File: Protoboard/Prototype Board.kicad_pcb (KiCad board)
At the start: 2 copper layers, 99.1 x 99.1 mm, 902 parts, among them J1 Conn_01x03_Male, J10 Conn_01x01, J11 Conn_01x01, J12 Conn_01x01, J13 Conn_01x01, J14 Conn_01x01, J15 Conn_01x01, J16 Conn_01x01, J17 Conn_01x01, J18 Conn_01x01, J19 Conn_01x01, J2 Conn_01x03_Male, J20 Conn_01x01, J21 Conn_01x01, J22 Conn_01x01, J23 Conn_01x01, J24 Conn_01x01, J25 Conn_01x01, J26 Conn_01x01, J27 Conn_01x01, J28 Conn_01x01, J29 Conn_01x01, J3 Conn_01x03_Male, J30 Conn_01x01, J31 Conn_01x01, J32 Conn_01x01, J33 Conn_01x01, J34 Conn_01x01, J4 Conn_01x03_Male, J5 Conn_01x01, J6 Conn_01x01, J7 Conn_01x01, J8 Conn_01x01, J9 Conn_01x01, SW1 SW_Push_Dual, SW2 SW_Push_Dual, SW3 SW_Push_Dual, SW4 SW_Push_Dual, SW5 SW_Push_Dual, SW6 SW_Push_Dual

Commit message: Protoboard edits
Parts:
- removed the G*** at (139.7, 35.6)

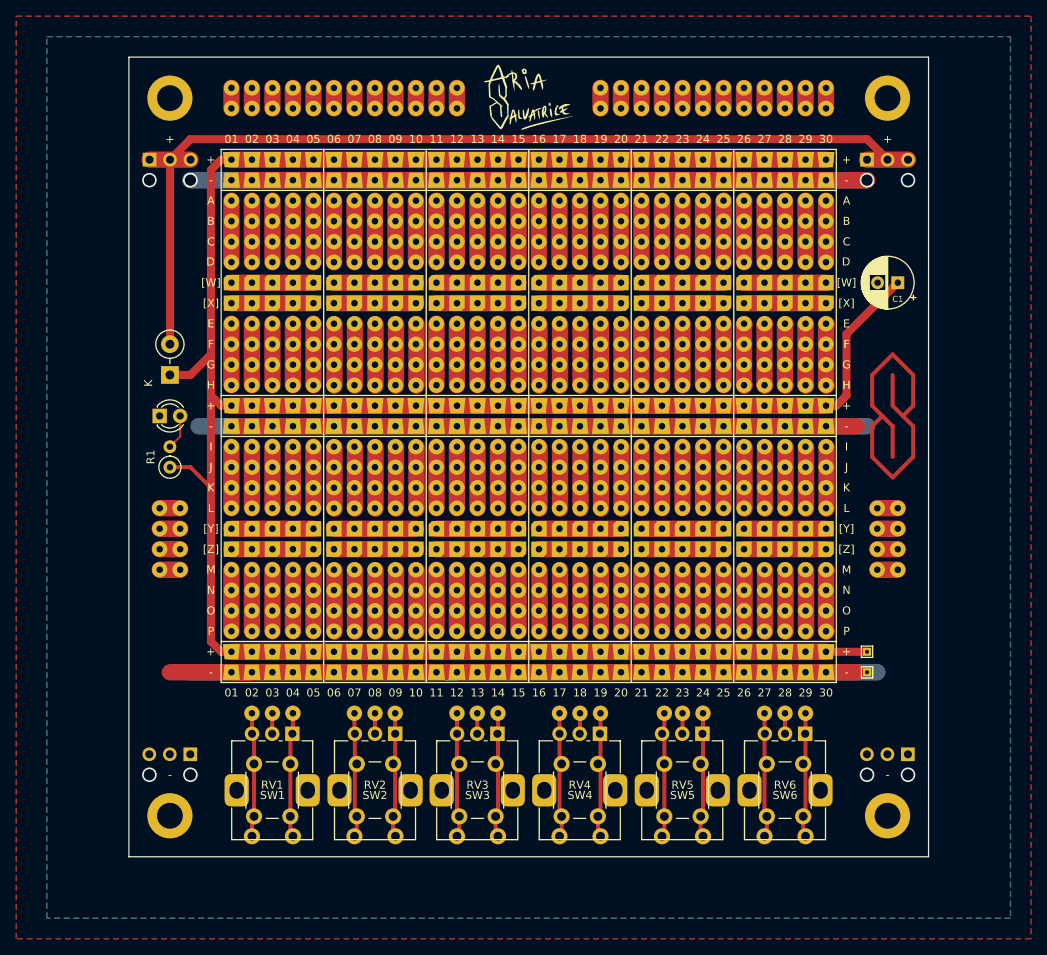
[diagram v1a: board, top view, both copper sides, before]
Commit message: Improve Protoboard Rev2
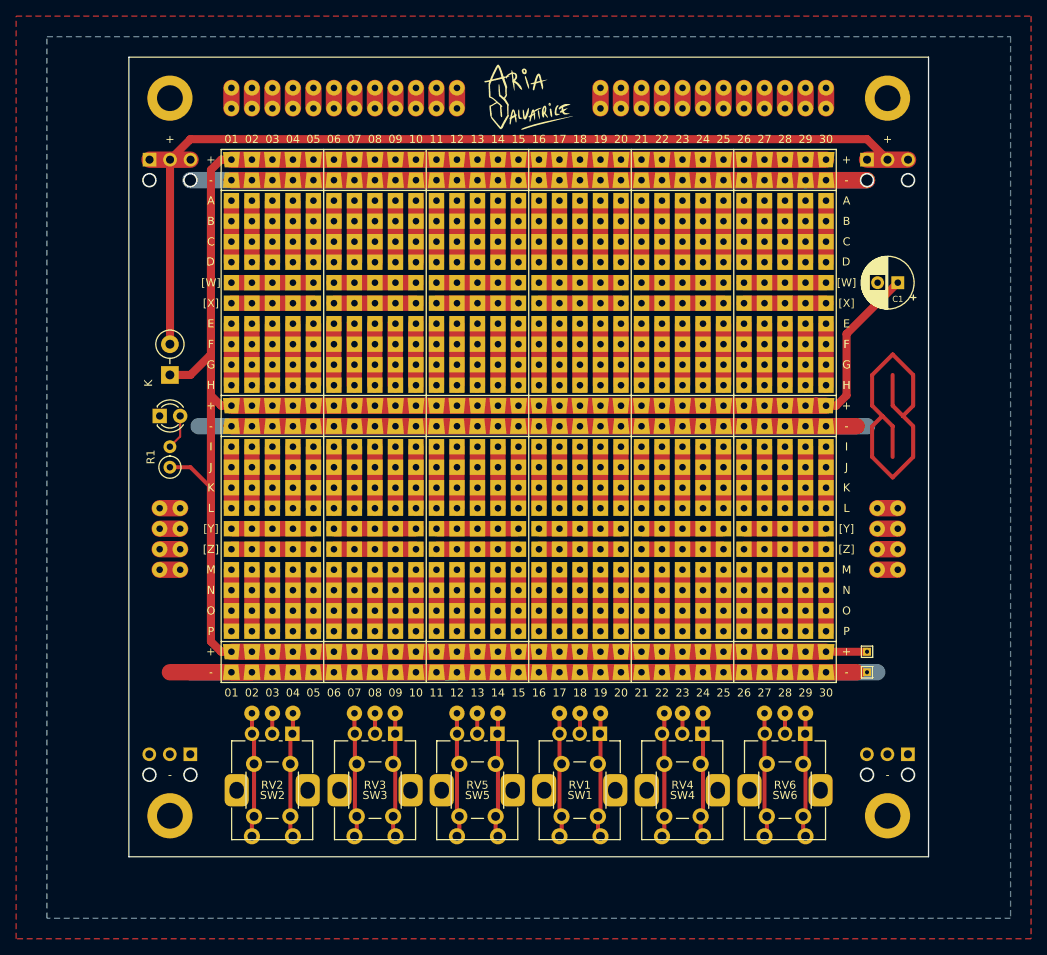
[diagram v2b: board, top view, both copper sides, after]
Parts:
- removed the REF** at (104.1, 78.7)
- removed the REF** at (104.1, 48.3)
- removed REF**1 (x2), REF**10 (x2), REF**100 (x2), REF**101 (x2), REF**102 (x2), REF**103 (x2), REF**104 (x2), REF**105 (x2), REF**106 (x2), REF**107 (x2), REF**108 (x2), REF**109 (x2), REF**11 (x2), REF**110 (x2), REF**111 (x2), REF**112 (x2), REF**113 (x2), REF**114 (x2), REF**115 (x2), REF**116 (x2), REF**117 (x2), REF**118 (x2), REF**119 (x2), REF**12 (x2), REF**120 (x2), REF**121 (x2), REF**122 (x2), REF**123 (x2), REF**124 (x2), REF**125 (x2), REF**126 (x2), REF**127 (x2), REF**128 (x2), REF**129 (x2), REF**13 (x2), REF**130 (x2), REF**131 (x2), REF**132 (x2), REF**133 (x2), REF**134 (x2), REF**135 (x2), REF**136 (x2), REF**137 (x2), REF**138 (x2), REF**139 (x2), REF**14 (x2), REF**140 (x2), REF**141 (x2), REF**142 (x2), REF**143 (x2), REF**144 (x2), REF**145 (x2), REF**146 (x2), REF**147 (x2), REF**148 (x2), REF**149 (x2), REF**15 (x2), REF**150 (x2), REF**151 (x2), REF**152 (x2), REF**153 (x2), REF**154 (x2), REF**155 (x2), REF**156 (x2), REF**157 (x2), REF**158 (x2), REF**159 (x2), REF**16 (x2), REF**160 (x2), REF**161 (x2), REF**162 (x2), REF**163 (x2), REF**164 (x2), REF**165 (x2), REF**166 (x2), REF**167 (x2), REF**168 (x2), REF**169 (x2), REF**17 (x2), REF**170 (x2), REF**171 (x2), REF**172 (x2), REF**173 (x2), REF**174 (x2), REF**175 (x2), REF**176 (x2), REF**177 (x2), REF**178 (x2), REF**179 (x2), REF**18 (x2), REF**180 (x2), REF**181 (x2), REF**182 (x2), REF**183 (x2), REF**184 (x2), REF**185 (x2), REF**186 (x2), REF**187 (x2), REF**188 (x2), REF**189 (x2), REF**19 (x2), REF**190 (x2), REF**191 (x2), REF**192 (x2), REF**193 (x2), REF**194 (x2), REF**195 (x2), REF**196 (x2), REF**197 (x2), REF**198 (x2), REF**199 (x2), REF**2 (x2), REF**20 (x2), REF**200 (x2), REF**201 (x2), REF**202 (x2), REF**203 (x2), REF**204 (x2), REF**205 (x2), REF**206 (x2), REF**207 (x2), REF**208 (x2), REF**209 (x2), REF**21 (x2), REF**210 (x2), REF**211 (x2), REF**212 (x2), REF**213 (x2), REF**214 (x2), REF**215 (x2), REF**216 (x2), REF**217 (x2), REF**218 (x2), REF**219 (x2), REF**22 (x2), REF**220 (x2), REF**221 (x2), REF**222 (x2), REF**223 (x2), REF**224 (x2), REF**225 (x2), REF**226 (x2), REF**227 (x2), REF**228 (x2), REF**229 (x2), REF**23 (x2), REF**230 (x2), REF**231 (x2), REF**232 (x2), REF**233 (x2), REF**234 (x2), REF**235 (x2), REF**236 (x2), REF**237 (x2), REF**238 (x2), REF**239 (x2), REF**24 (x2), REF**240 (x2), REF**241 (x2), REF**242 (x2), REF**243 (x2), REF**244 (x2), REF**245 (x2), REF**246 (x2), REF**247 (x2), REF**248 (x2), REF**249 (x2), REF**25 (x2), REF**250 (x2), REF**251 (x2), REF**252 (x2), REF**253 (x2), REF**254 (x2), REF**255 (x2), REF**256 (x2), REF**257 (x2), REF**258 (x2), REF**259 (x2), REF**26 (x2), REF**260 (x2), REF**261 (x2), REF**262 (x2), REF**263 (x2), REF**264 (x2), REF**265 (x2), REF**266 (x2), REF**267 (x2), REF**268 (x2), REF**269 (x2), REF**27 (x2), REF**270 (x2), REF**271 (x2), REF**272 (x2), REF**273 (x2), REF**274 (x2), REF**275 (x2), REF**276 (x2), REF**277 (x2), REF**278 (x2), REF**279 (x2), REF**28 (x2), REF**280 (x2), REF**281 (x2), REF**282 (x2), REF**283 (x2), REF**284 (x2), REF**285 (x2), REF**286 (x2), REF**287 (x2), REF**288 (x2), REF**289 (x2), REF**29 (x2), REF**290 (x2), REF**291 (x2), REF**292 (x2), REF**293 (x2), REF**294 (x2), REF**295 (x2), REF**296 (x2), REF**297 (x2), REF**298 (x2), REF**299 (x2), REF**3 (x2), REF**30 (x2), REF**31 (x2), REF**32 (x2), REF**33 (x2), REF**34 (x2), REF**35 (x2), REF**36 (x2), REF**37 (x2), REF**38 (x2), REF**39 (x2), REF**4 (x2), REF**40 (x2), REF**41 (x2), REF**42 (x2), REF**43 (x2), REF**44 (x2), REF**45 (x2), REF**46 (x2), REF**47 (x2), REF**48 (x2), REF**49 (x2), REF**5 (x2), REF**50 (x2), REF**51 (x2), REF**52 (x2), REF**53 (x2), REF**54 (x2), REF**55 (x2), REF**56 (x2), REF**57 (x2), REF**58 (x2), REF**59 (x2), REF**6 (x2), REF**60 (x2), REF**61 (x2), REF**62 (x2), REF**63 (x2), REF**64 (x2), REF**65 (x2), REF**66 (x2), REF**67 (x2), REF**68 (x2), REF**69 (x2), REF**7 (x2), REF**70 (x2), REF**71 (x2), REF**72 (x2), REF**73 (x2), REF**74 (x2), REF**75 (x2), REF**76 (x2), REF**77 (x2), REF**78 (x2), REF**79 (x2), REF**8 (x2), REF**80 (x2), REF**81 (x2), REF**82 (x2), REF**83 (x2), REF**84 (x2), REF**85 (x2), REF**86 (x2), REF**87 (x2), REF**88 (x2), REF**89 (x2), REF**9 (x2), REF**90 (x2), REF**91 (x2), REF**92 (x2), REF**93 (x2), REF**94 (x2), REF**95 (x2), REF**96 (x2), REF**97 (x2), REF**98 (x2), REF**99 (x2): PBH, ao_tht:Perf_Board_Hole
- added J100: Connectable_Pad_Group_01x04, Protoboard:Connectable_Pad_Group_01x04, F.Cu at (111.8, 78.7)
- added J101: Connectable_Pad_Group_01x04, Protoboard:Connectable_Pad_Group_01x04, F.Cu at (114.3, 78.7)
- added J102: Connectable_Pad_Group_01x04, Protoboard:Connectable_Pad_Group_01x04, F.Cu at (116.8, 78.7)
- added J103: Connectable_Pad_Group_01x04, Protoboard:Connectable_Pad_Group_01x04, F.Cu at (119.4, 78.7)
- added J104: Connectable_Pad_Group_01x04, Protoboard:Connectable_Pad_Group_01x04, F.Cu at (121.9, 78.7)
- added J105: Connectable_Pad_Group_01x04, Protoboard:Connectable_Pad_Group_01x04, F.Cu at (124.5, 78.7)
- added J106: Connectable_Pad_Group_01x04, Protoboard:Connectable_Pad_Group_01x04, F.Cu at (127.0, 78.7)
- added J107: Connectable_Pad_Group_01x04, Protoboard:Connectable_Pad_Group_01x04, F.Cu at (129.5, 78.7)
- added J108: Connectable_Pad_Group_01x04, Protoboard:Connectable_Pad_Group_01x04, F.Cu at (132.1, 78.7)
- added J109: Connectable_Pad_Group_01x04, Protoboard:Connectable_Pad_Group_01x04, F.Cu at (134.6, 78.7)
- added J110: Connectable_Pad_Group_01x04, Protoboard:Connectable_Pad_Group_01x04, F.Cu at (137.2, 78.7)
- added J111: Connectable_Pad_Group_01x04, Protoboard:Connectable_Pad_Group_01x04, F.Cu at (139.7, 78.7)
- added J112: Connectable_Pad_Group_01x04, Protoboard:Connectable_Pad_Group_01x04, F.Cu at (142.2, 78.7)
- added J113: Connectable_Pad_Group_01x04, Protoboard:Connectable_Pad_Group_01x04, F.Cu at (144.8, 78.7)
- added J114: Connectable_Pad_Group_01x04, Protoboard:Connectable_Pad_Group_01x04, F.Cu at (147.3, 78.7)
- added J115: Connectable_Pad_Group_01x04, Protoboard:Connectable_Pad_Group_01x04, F.Cu at (149.9, 78.7)
- added J116: Connectable_Pad_Group_01x04, Protoboard:Connectable_Pad_Group_01x04, F.Cu at (152.4, 78.7)
- added J117: Connectable_Pad_Group_01x04, Protoboard:Connectable_Pad_Group_01x04, F.Cu at (154.9, 78.7)
- added J118: Connectable_Pad_Group_01x04, Protoboard:Connectable_Pad_Group_01x04, F.Cu at (157.5, 78.7)
- added J119: Connectable_Pad_Group_01x04, Protoboard:Connectable_Pad_Group_01x04, F.Cu at (160.0, 78.7)
- added J120: Connectable_Pad_Group_01x04, Protoboard:Connectable_Pad_Group_01x04, F.Cu at (162.6, 78.7)
- added J121: Connectable_Pad_Group_01x04, Protoboard:Connectable_Pad_Group_01x04, F.Cu at (165.1, 78.7)
- added J122: Connectable_Pad_Group_01x04, Protoboard:Connectable_Pad_Group_01x04, F.Cu at (167.6, 78.7)
- added J123: Connectable_Pad_Group_01x04, Protoboard:Connectable_Pad_Group_01x04, F.Cu at (170.2, 78.7)
- added J124: Connectable_Pad_Group_01x04, Protoboard:Connectable_Pad_Group_01x04, F.Cu at (172.7, 78.7)
- added J125: Connectable_Pad_Group_01x04, Protoboard:Connectable_Pad_Group_01x04, F.Cu at (175.3, 78.7)
- added J126: Connectable_Pad_Group_01x04, Protoboard:Connectable_Pad_Group_01x04, F.Cu at (177.8, 78.7)
- added J127: ~, Protoboard:Connectable_Pad_Group_02x05, F.Cu at (104.1, 88.9)
- added J128: ~, Protoboard:Connectable_Pad_Group_02x05, F.Cu at (116.8, 88.9)
- added J129: ~, Protoboard:Connectable_Pad_Group_02x05, F.Cu at (129.5, 88.9)
- added J130: ~, Protoboard:Connectable_Pad_Group_02x05, F.Cu at (142.2, 88.9)
- added J131: ~, Protoboard:Connectable_Pad_Group_02x05, F.Cu at (154.9, 88.9)
- added J132: ~, Protoboard:Connectable_Pad_Group_02x05, F.Cu at (167.6, 88.9)
- added J135: Connectable_Pad_Group_01x04, Protoboard:Connectable_Pad_Group_01x04, F.Cu at (104.1, 94.0)
- added J136: Connectable_Pad_Group_01x04, Protoboard:Connectable_Pad_Group_01x04, F.Cu at (106.7, 94.0)
- added J137: Connectable_Pad_Group_01x04, Protoboard:Connectable_Pad_Group_01x04, F.Cu at (109.2, 94.0)
- added J138: Connectable_Pad_Group_01x04, Protoboard:Connectable_Pad_Group_01x04, F.Cu at (111.8, 94.0)
- added J139: Connectable_Pad_Group_01x04, Protoboard:Connectable_Pad_Group_01x04, F.Cu at (114.3, 94.0)
- added J140: Connectable_Pad_Group_01x04, Protoboard:Connectable_Pad_Group_01x04, F.Cu at (116.8, 94.0)
- added J141: Connectable_Pad_Group_01x04, Protoboard:Connectable_Pad_Group_01x04, F.Cu at (119.4, 94.0)
- added J142: Connectable_Pad_Group_01x04, Protoboard:Connectable_Pad_Group_01x04, F.Cu at (121.9, 94.0)
- added J143: Connectable_Pad_Group_01x04, Protoboard:Connectable_Pad_Group_01x04, F.Cu at (124.5, 94.0)
- added J144: Connectable_Pad_Group_01x04, Protoboard:Connectable_Pad_Group_01x04, F.Cu at (127.0, 94.0)
- added J145: Connectable_Pad_Group_01x04, Protoboard:Connectable_Pad_Group_01x04, F.Cu at (129.5, 94.0)
- added J146: Connectable_Pad_Group_01x04, Protoboard:Connectable_Pad_Group_01x04, F.Cu at (132.1, 94.0)
- added J147: Connectable_Pad_Group_01x04, Protoboard:Connectable_Pad_Group_01x04, F.Cu at (134.6, 94.0)
- added J148: Connectable_Pad_Group_01x04, Protoboard:Connectable_Pad_Group_01x04, F.Cu at (137.2, 94.0)
- added J149: Connectable_Pad_Group_01x04, Protoboard:Connectable_Pad_Group_01x04, F.Cu at (139.7, 94.0)
- added J150: Connectable_Pad_Group_01x04, Protoboard:Connectable_Pad_Group_01x04, F.Cu at (142.2, 94.0)
- added J151: Connectable_Pad_Group_01x04, Protoboard:Connectable_Pad_Group_01x04, F.Cu at (144.8, 94.0)
- added J152: Connectable_Pad_Group_01x04, Protoboard:Connectable_Pad_Group_01x04, F.Cu at (147.3, 94.0)
- added J153: Connectable_Pad_Group_01x04, Protoboard:Connectable_Pad_Group_01x04, F.Cu at (149.9, 94.0)
- added J154: Connectable_Pad_Group_01x04, Protoboard:Connectable_Pad_Group_01x04, F.Cu at (152.4, 94.0)
- added J155: Connectable_Pad_Group_01x04, Protoboard:Connectable_Pad_Group_01x04, F.Cu at (154.9, 94.0)
- added J156: Connectable_Pad_Group_01x04, Protoboard:Connectable_Pad_Group_01x04, F.Cu at (157.5, 94.0)
- added J157: Connectable_Pad_Group_01x04, Protoboard:Connectable_Pad_Group_01x04, F.Cu at (160.0, 94.0)
- added J158: Connectable_Pad_Group_01x04, Protoboard:Connectable_Pad_Group_01x04, F.Cu at (162.6, 94.0)
- added J159: Connectable_Pad_Group_01x04, Protoboard:Connectable_Pad_Group_01x04, F.Cu at (165.1, 94.0)
- added J160: Connectable_Pad_Group_01x04, Protoboard:Connectable_Pad_Group_01x04, F.Cu at (167.6, 94.0)
- added J161: Connectable_Pad_Group_01x04, Protoboard:Connectable_Pad_Group_01x04, F.Cu at (170.2, 94.0)
- added J162: Connectable_Pad_Group_01x04, Protoboard:Connectable_Pad_Group_01x04, F.Cu at (172.7, 94.0)
- added J163: Connectable_Pad_Group_01x04, Protoboard:Connectable_Pad_Group_01x04, F.Cu at (175.3, 94.0)
- added J164: Connectable_Pad_Group_01x04, Protoboard:Connectable_Pad_Group_01x04, F.Cu at (177.8, 94.0)
- added J17: Connectable_Pad_Group_01x04, Protoboard:Connectable_Pad_Group_01x04, F.Cu at (104.1, 48.3)
- added J18: Connectable_Pad_Group_01x04, Protoboard:Connectable_Pad_Group_01x04, F.Cu at (106.7, 48.3)
- added J19: Connectable_Pad_Group_01x04, Protoboard:Connectable_Pad_Group_01x04, F.Cu at (109.2, 48.3)
- added J20: Connectable_Pad_Group_01x04, Protoboard:Connectable_Pad_Group_01x04, F.Cu at (111.8, 48.3)
- added J21: Connectable_Pad_Group_01x04, Protoboard:Connectable_Pad_Group_01x04, F.Cu at (114.3, 48.3)
- added J22: Connectable_Pad_Group_01x04, Protoboard:Connectable_Pad_Group_01x04, F.Cu at (116.8, 48.3)
- added J23: Connectable_Pad_Group_01x04, Protoboard:Connectable_Pad_Group_01x04, F.Cu at (119.4, 48.3)
- added J24: Connectable_Pad_Group_01x04, Protoboard:Connectable_Pad_Group_01x04, F.Cu at (121.9, 48.3)
- added J25: Connectable_Pad_Group_01x04, Protoboard:Connectable_Pad_Group_01x04, F.Cu at (124.5, 48.3)
- added J26: Connectable_Pad_Group_01x04, Protoboard:Connectable_Pad_Group_01x04, F.Cu at (127.0, 48.3)
- added J27: Connectable_Pad_Group_01x04, Protoboard:Connectable_Pad_Group_01x04, F.Cu at (129.5, 48.3)
- added J28: Connectable_Pad_Group_01x04, Protoboard:Connectable_Pad_Group_01x04, F.Cu at (132.1, 48.3)
- added J29: Connectable_Pad_Group_01x04, Protoboard:Connectable_Pad_Group_01x04, F.Cu at (134.6, 48.3)
- added J30: Connectable_Pad_Group_01x04, Protoboard:Connectable_Pad_Group_01x04, F.Cu at (137.2, 48.3)
- added J31: Connectable_Pad_Group_01x04, Protoboard:Connectable_Pad_Group_01x04, F.Cu at (139.7, 48.3)
- added J32: Connectable_Pad_Group_01x04, Protoboard:Connectable_Pad_Group_01x04, F.Cu at (142.2, 48.3)
- added J33: Connectable_Pad_Group_01x04, Protoboard:Connectable_Pad_Group_01x04, F.Cu at (144.8, 48.3)
- added J34: Connectable_Pad_Group_01x04, Protoboard:Connectable_Pad_Group_01x04, F.Cu at (147.3, 48.3)
- added J35: Connectable_Pad_Group_01x04, Protoboard:Connectable_Pad_Group_01x04, F.Cu at (149.9, 48.3)
- added J36: Connectable_Pad_Group_01x04, Protoboard:Connectable_Pad_Group_01x04, F.Cu at (152.4, 48.3)
- added J37: Connectable_Pad_Group_01x04, Protoboard:Connectable_Pad_Group_01x04, F.Cu at (154.9, 48.3)
- added J38: Connectable_Pad_Group_01x04, Protoboard:Connectable_Pad_Group_01x04, F.Cu at (157.5, 48.3)
- added J39: Connectable_Pad_Group_01x04, Protoboard:Connectable_Pad_Group_01x04, F.Cu at (160.0, 48.3)
- added J40: Connectable_Pad_Group_01x04, Protoboard:Connectable_Pad_Group_01x04, F.Cu at (162.6, 48.3)
- added J41: Connectable_Pad_Group_01x04, Protoboard:Connectable_Pad_Group_01x04, F.Cu at (165.1, 48.3)
- added J42: Connectable_Pad_Group_01x04, Protoboard:Connectable_Pad_Group_01x04, F.Cu at (167.6, 48.3)
- added J43: Connectable_Pad_Group_01x04, Protoboard:Connectable_Pad_Group_01x04, F.Cu at (170.2, 48.3)
- added J44: Connectable_Pad_Group_01x04, Protoboard:Connectable_Pad_Group_01x04, F.Cu at (172.7, 48.3)
- added J45: Connectable_Pad_Group_01x04, Protoboard:Connectable_Pad_Group_01x04, F.Cu at (175.3, 48.3)
- added J46: Connectable_Pad_Group_01x04, Protoboard:Connectable_Pad_Group_01x04, F.Cu at (177.8, 48.3)
- added J55: ~, Protoboard:Connectable_Pad_Group_02x05, F.Cu at (104.1, 58.4)
- added J56: ~, Protoboard:Connectable_Pad_Group_02x05, F.Cu at (116.8, 58.4)
- added J57: ~, Protoboard:Connectable_Pad_Group_02x05, F.Cu at (129.5, 58.4)
- added J58: ~, Protoboard:Connectable_Pad_Group_02x05, F.Cu at (142.2, 58.4)
- added J59: ~, Protoboard:Connectable_Pad_Group_02x05, F.Cu at (154.9, 58.4)
- added J60: ~, Protoboard:Connectable_Pad_Group_02x05, F.Cu at (167.6, 58.4)
- added J63: Connectable_Pad_Group_01x04, Protoboard:Connectable_Pad_Group_01x04, F.Cu at (104.1, 63.5)
- added J64: Connectable_Pad_Group_01x04, Protoboard:Connectable_Pad_Group_01x04, F.Cu at (106.7, 63.5)
- added J65: Connectable_Pad_Group_01x04, Protoboard:Connectable_Pad_Group_01x04, F.Cu at (109.2, 63.5)
- added J66: Connectable_Pad_Group_01x04, Protoboard:Connectable_Pad_Group_01x04, F.Cu at (111.8, 63.5)
- added J67: Connectable_Pad_Group_01x04, Protoboard:Connectable_Pad_Group_01x04, F.Cu at (114.3, 63.5)
- added J68: Connectable_Pad_Group_01x04, Protoboard:Connectable_Pad_Group_01x04, F.Cu at (116.8, 63.5)
- added J69: Connectable_Pad_Group_01x04, Protoboard:Connectable_Pad_Group_01x04, F.Cu at (119.4, 63.5)
- added J70: Connectable_Pad_Group_01x04, Protoboard:Connectable_Pad_Group_01x04, F.Cu at (121.9, 63.5)
- added J71: Connectable_Pad_Group_01x04, Protoboard:Connectable_Pad_Group_01x04, F.Cu at (124.5, 63.5)
- added J72: Connectable_Pad_Group_01x04, Protoboard:Connectable_Pad_Group_01x04, F.Cu at (127.0, 63.5)
- added J73: Connectable_Pad_Group_01x04, Protoboard:Connectable_Pad_Group_01x04, F.Cu at (129.5, 63.5)
- added J74: Connectable_Pad_Group_01x04, Protoboard:Connectable_Pad_Group_01x04, F.Cu at (132.1, 63.5)
- added J75: Connectable_Pad_Group_01x04, Protoboard:Connectable_Pad_Group_01x04, F.Cu at (134.6, 63.5)
- added J76: Connectable_Pad_Group_01x04, Protoboard:Connectable_Pad_Group_01x04, F.Cu at (137.2, 63.5)
- added J77: Connectable_Pad_Group_01x04, Protoboard:Connectable_Pad_Group_01x04, F.Cu at (139.7, 63.5)
- added J78: Connectable_Pad_Group_01x04, Protoboard:Connectable_Pad_Group_01x04, F.Cu at (142.2, 63.5)
- added J79: Connectable_Pad_Group_01x04, Protoboard:Connectable_Pad_Group_01x04, F.Cu at (144.8, 63.5)
- added J80: Connectable_Pad_Group_01x04, Protoboard:Connectable_Pad_Group_01x04, F.Cu at (147.3, 63.5)
- added J81: Connectable_Pad_Group_01x04, Protoboard:Connectable_Pad_Group_01x04, F.Cu at (149.9, 63.5)
- added J82: Connectable_Pad_Group_01x04, Protoboard:Connectable_Pad_Group_01x04, F.Cu at (152.4, 63.5)
- renumbered D2 to D1, D1 to D2, J20 to J1, J12 to J10, J7 to J11, J13 to J12, J22 to J13, J1 to J133, J3 to J134, J28 to J14, J18 to J15, J33 to J16, J2 to J165, J4 to J166, J35 to J167, J41 to J168, J47 to J169, J53 to J170, J59 to J171, J65 to J172, J71 to J173, J77 to J174, J83 to J175, J89 to J176, J95 to J177, J101 to J178, J107 to J179, J113 to J180, J119 to J181, J125 to J182, J131 to J183, J137 to J184, J143 to J185, J149 to J186, J155 to J187, J161 to J188, J167 to J189, J173 to J190, J179 to J191, J185 to J192, J191 to J193, J197 to J194, J203 to J195, J209 to J196, J36 to J197, J42 to J198, J48 to J199, J26 to J2, J54 to J200, J60 to J201, J66 to J202, J72 to J203, J78 to J204, J84 to J205, J90 to J206, J96 to J207, J102 to J208, J108 to J209, J114 to J210, J120 to J211, J126 to J212, J132 to J213, J138 to J214, J144 to J215, J150 to J216, J156 to J217, J162 to J218, J168 to J219, J174 to J220, J180 to J221, J186 to J222, J192 to J223, J198 to J224, J204 to J225, J210 to J226, J37 to J227, J43 to J228, J49 to J229, J55 to J230, J61 to J231, J67 to J232, J73 to J233, J79 to J234, J85 to J235, J91 to J236, J97 to J237, J103 to J238, J109 to J239, J115 to J240, J121 to J241, J127 to J242, J133 to J243, J139 to J244, J145 to J245, J151 to J246, J157 to J247, J163 to J248, J169 to J249, J175 to J250, J181 to J251, J187 to J252, J193 to J253, J199 to J254, J205 to J255, J211 to J256, J38 to J257, J44 to J258, J50 to J259, J56 to J260, J62 to J261, J68 to J262, J74 to J263, J80 to J264, J86 to J265, J92 to J266, J98 to J267, J104 to J268, J110 to J269, J116 to J270, J122 to J271, J128 to J272, J134 to J273, J140 to J274, J146 to J275, J152 to J276, J158 to J277, J164 to J278, J170 to J279, J176 to J280, J182 to J281, J188 to J282, J194 to J283, J200 to J284, J206 to J285, J212 to J286, J39 to J287, J45 to J288, J51 to J289, J57 to J290, J63 to J291, J69 to J292, J75 to J293, J81 to J294, J87 to J295, J93 to J296, J99 to J297, J105 to J298, J111 to J299, J5 to J3, J117 to J300, J123 to J301, J129 to J302, J135 to J303, J141 to J304, J147 to J305, J153 to J306, J159 to J307, J165 to J308, J171 to J309, J177 to J310, J183 to J311, J189 to J312, J195 to J313, J201 to J314, J207 to J315, J213 to J316, J40 to J317, J46 to J318, J52 to J319, J58 to J320, J64 to J321, J70 to J322, J76 to J323, J82 to J324, J88 to J325, J94 to J326, J100 to J327, J106 to J328, J112 to J329, J118 to J330, J124 to J331, J130 to J332, J136 to J333, J142 to J334, J148 to J335, J154 to J336, J160 to J337, J166 to J338, J172 to J339, J178 to J340, J184 to J341, J190 to J342, J196 to J343, J202 to J344, J208 to J345, J214 to J346, J11 to J4, J8 to J47, J14 to J48, J23 to J49, J32 to J5, J29 to J50, J9 to J51, J15 to J52, J24 to J53, J30 to J54, J17 to J6, J19 to J61, J34 to J62, J21 to J7, J27 to J8, J6 to J9, J10 to J93, J16 to J94, J25 to J95, J31 to J96, RV4 to RV1, RV1 to RV2, RV2 to RV3, RV5 to RV4, RV3 to RV5, SW4 to SW1, SW1 to SW2, SW2 to SW3, SW5 to SW4, SW3 to SW5
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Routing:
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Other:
- board text added: "TODO LIST - Bonus pads not on the schematic - Imported symbol to replace - Rotary encoder?? - Remake the cursed footprints - Redo schematic - Have 3D models - Can I fit in MORE knobs? - Use proper net width (sounds complicated) - Pass DRC lol"
- board text removed: "TODO LIST - Vertical tracks are poorly aligned - Vertical tracks are not on the schematic - Horizontal groups poorly separated visually - Horizontal groups are not on the schematic - Bonus pads not on the schematic - Imported symbol to replace - Move capacitor up? - Rotary encoder?? - Remake the cursed footprints - Redo schematic - Have 3D models - Can I fit in MORE knobs? - Use proper net width 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"

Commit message: Protoboard Rev2 ready soon, needs checking
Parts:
- removed the J167 at (170.2, 43.2)
- removed J168, J169, J170, J171, J172, J173, J193, J194, J195, J196, J197, J198, J214, J215, J216, J217, J218, J219, J220, J221, J222, J223, J224, J225, J226, J227, J228, J229, J230, J231, J232, J233, J234, J235, J236, J237, J238, J239, J240, J241, J242, J243, J244, J245, J246, J247, J248, J249, J250, J251, J252, J253, J254, J255, J256, J257, J258, J259, J260, J261, J262, J263, J264, J265, J266, J267, J268, J269, J270, J271, J272, J273, J274, J275, J276, J277, J278, J279, J280, J281, J282, J283, J284, J285, J286, J287, J288, J289, J290, J291, J292, J293, J294, J295, J296, J297, J298, J299, J300, J301, J302, J303, J304, J305, J306, J307, J308, J309, J310, J311, J312, J313, J314, J315, J316, J317, J318, J319, J320, J321, J322, J323, J324, J325, J326, J327, J328, J329, J330, J331, J332, J333, J334, J335, J336, J337, J338, J339, J340, J341, J342, J343, J344, J345, J346: ~, ao_tht:Perf_Board_Hole
- removed the J174 at (167.6, 43.2)
- removed the J175 at (127.0, 43.2)
- removed the J176 at (142.2, 43.2)
- removed the J177 at (114.3, 43.2)
- removed the J178 at (116.8, 43.2)
- removed the J179 at (149.9, 43.2)
- removed the J180 at (106.7, 43.2)
- removed the J181 at (147.3, 43.2)
- removed the J182 at (172.7, 43.2)
- removed the J183 at (154.9, 43.2)
- removed the J184 at (124.5, 43.2)
- removed the J185 at (119.4, 43.2)
- removed the J186 at (144.8, 43.2)
- removed the J187 at (109.2, 43.2)
- removed the J188 at (152.4, 43.2)
- removed the J189 at (139.7, 43.2)
- removed the J190 at (162.6, 43.2)
- removed the J191 at (132.1, 43.2)
- removed the J192 at (160.0, 43.2)
- removed the J199 at (165.1, 45.7)
- removed the J200 at (137.2, 45.7)
- removed the J201 at (116.8, 45.7)
- removed the J202 at (144.8, 45.7)
- removed the J203 at (127.0, 45.7)
- removed the J204 at (157.5, 45.7)
- removed the J205 at (149.9, 45.7)
- removed the J206 at (124.5, 45.7)
- removed the J207 at (114.3, 45.7)
- removed the J208 at (175.3, 45.7)
- removed the J209 at (104.1, 45.7)
- removed the J210 at (139.7, 45.7)
- removed the J211 at (106.7, 45.7)
- removed the J212 at (160.0, 45.7)
- removed the J213 at (109.2, 45.7)
- removed the REF** at (177.8, 34.3)
- removed the REF** at (132.1, 34.3)
- removed the REF** at (95.2, 91.4)
- removed the REF** at (121.9, 36.8)
- removed the REF** at (152.4, 34.3)
- removed the REF** at (184.2, 94.0)
- removed the REF** at (97.8, 91.4)
- removed the REF** at (167.6, 36.8)
- removed the REF** at (97.8, 94.0)
- removed the REF** at (152.4, 36.8)
- removed the REF** at (114.3, 34.3)
- removed the REF** at (160.0, 34.3)
- removed the REF** at (184.2, 88.9)
- removed the REF** at (175.3, 36.8)
- removed the REF** at (172.7, 34.3)
- removed the REF** at (95.2, 86.4)
- removed the REF** at (170.2, 34.3)
- removed the REF** at (129.5, 34.3)
- removed the REF** at (175.3, 34.3)
- removed the REF** at (154.9, 34.3)
- removed the REF** at (109.2, 34.3)
- removed the REF** at (111.8, 34.3)
- removed the REF** at (119.4, 34.3)
- removed the REF** at (116.8, 34.3)
- removed the REF** at (165.1, 36.8)
- removed the REF** at (184.2, 91.4)
- removed the REF** at (119.4, 36.8)
- removed the REF** at (157.5, 36.8)
- removed the REF** at (160.0, 36.8)
- removed the REF** at (186.7, 94.0)
- removed the REF** at (170.2, 36.8)
- removed the REF** at (154.9, 36.8)
- removed the REF** at (132.1, 36.8)
- removed the REF** at (124.5, 36.8)
- removed the REF** at (95.2, 88.9)
- removed the REF** at (127.0, 36.8)
- removed the REF** at (172.7, 36.8)
- removed the REF** at (149.9, 34.3)
- removed the REF** at (111.8, 36.8)
- removed the REF** at (186.7, 91.4)
- removed the REF** at (97.8, 86.4)
- removed the REF** at (106.7, 34.3)
- removed the REF** at (129.5, 36.8)
- removed the REF** at (177.8, 36.8)
- removed the REF** at (186.7, 86.4)
- removed the REF** at (116.8, 36.8)
- removed the REF** at (97.8, 88.9)
- removed the REF** at (186.7, 88.9)
- removed the REF** at (104.1, 34.3)
- removed the REF** at (109.2, 36.8)
- removed the REF** at (124.5, 34.3)
- removed the REF** at (106.7, 36.8)
- removed the REF** at (167.6, 34.3)
- removed the REF** at (104.1, 36.8)
- removed the REF** at (95.2, 94.0)
- removed the REF** at (121.9, 34.3)
- removed the REF** at (127.0, 34.3)
- removed the REF** at (114.3, 36.8)
- removed the REF** at (157.5, 34.3)
- removed the REF** at (184.2, 86.4)
- removed the REF** at (162.6, 34.3)
- removed the REF** at (165.1, 34.3)
- removed the REF** at (149.9, 36.8)
- removed the REF** at (162.6, 36.8)
- added J1: Connectable_Pad_Group_01x02, Protoboard:Connectable_Pad_Group_01x02, F.Cu at (97.8, 86.4)
- added J103: Connectable_Pad_Group_01x02, Protoboard:Connectable_Pad_Group_01x02, F.Cu at (157.5, 34.3)
- added J11: Power_Rail_30, Protoboard:Power_Rail_30, F.Cu at (104.1, 43.2)
- added J112: Connectable_Pad_Group_01x02, Protoboard:Connectable_Pad_Group_01x02, F.Cu at (160.0, 34.3)
- added J113: Connectable_Pad_Group_01x02, Protoboard:Connectable_Pad_Group_01x02, F.Cu at (162.6, 34.3)
- added J124: Connectable_Pad_Group_01x02, Protoboard:Connectable_Pad_Group_01x02, F.Cu at (165.1, 34.3)
- added J129: Connectable_Pad_Group_01x02, Protoboard:Connectable_Pad_Group_01x02, F.Cu at (167.6, 34.3)
- added J13: Power_Rail_30, Protoboard:Power_Rail_30, F.Cu at (104.1, 73.7)
- added J134: Connectable_Pad_Group_01x02, Protoboard:Connectable_Pad_Group_01x02, F.Cu at (170.2, 34.3)
- added J139: Connectable_Pad_Group_01x02, Protoboard:Connectable_Pad_Group_01x02, F.Cu at (172.7, 34.3)
- added J146: Connectable_Pad_Group_01x02, Protoboard:Connectable_Pad_Group_01x02, F.Cu at (175.3, 34.3)
- added J15: Power_Rail_30, Protoboard:Power_Rail_30, F.Cu at (104.1, 104.1)
- added J151: Connectable_Pad_Group_01x02, Protoboard:Connectable_Pad_Group_01x02, F.Cu at (186.7, 86.4)
- added J152: Connectable_Pad_Group_01x02, Protoboard:Connectable_Pad_Group_01x02, F.Cu at (186.7, 88.9)
- added J153: Connectable_Pad_Group_01x02, Protoboard:Connectable_Pad_Group_01x02, F.Cu at (186.7, 91.4)
- added J154: Connectable_Pad_Group_01x02, Protoboard:Connectable_Pad_Group_01x02, F.Cu at (186.7, 94.0)
- added J159: Connectable_Pad_Group_01x02, Protoboard:Connectable_Pad_Group_01x02, F.Cu at (177.8, 34.3)
- added J16: Connectable_Pad_Group_01x02, Protoboard:Connectable_Pad_Group_01x02, F.Cu at (109.2, 34.3)
- added J2: Connectable_Pad_Group_01x02, Protoboard:Connectable_Pad_Group_01x02, F.Cu at (97.8, 88.9)
- added J25: Connectable_Pad_Group_01x02, Protoboard:Connectable_Pad_Group_01x02, F.Cu at (111.8, 34.3)
- added J3: Connectable_Pad_Group_01x02, Protoboard:Connectable_Pad_Group_01x02, F.Cu at (97.8, 91.4)
- added J30: Connectable_Pad_Group_01x02, Protoboard:Connectable_Pad_Group_01x02, F.Cu at (114.3, 34.3)
- added J35: Connectable_Pad_Group_01x02, Protoboard:Connectable_Pad_Group_01x02, F.Cu at (116.8, 34.3)
- added J4: Connectable_Pad_Group_01x02, Protoboard:Connectable_Pad_Group_01x02, F.Cu at (97.8, 94.0)
- added J42: Connectable_Pad_Group_01x02, Protoboard:Connectable_Pad_Group_01x02, F.Cu at (119.4, 34.3)
- added J47: Connectable_Pad_Group_01x02, Protoboard:Connectable_Pad_Group_01x02, F.Cu at (121.9, 34.3)
- added J5: Connectable_Pad_Group_01x02, Protoboard:Connectable_Pad_Group_01x02, F.Cu at (104.1, 34.3)
- added J56: Connectable_Pad_Group_01x02, Protoboard:Connectable_Pad_Group_01x02, F.Cu at (124.5, 34.3)
- added J6: Connectable_Pad_Group_01x02, Protoboard:Connectable_Pad_Group_01x02, F.Cu at (106.7, 34.3)
- added J61: Connectable_Pad_Group_01x02, Protoboard:Connectable_Pad_Group_01x02, F.Cu at (127.0, 34.3)
- added J62: Connectable_Pad_Group_01x02, Protoboard:Connectable_Pad_Group_01x02, F.Cu at (129.5, 34.3)
- added J73: Connectable_Pad_Group_01x02, Protoboard:Connectable_Pad_Group_01x02, F.Cu at (132.1, 34.3)
- added J86: Connectable_Pad_Group_01x02, Protoboard:Connectable_Pad_Group_01x02, F.Cu at (149.9, 34.3)
- added J91: Connectable_Pad_Group_01x02, Protoboard:Connectable_Pad_Group_01x02, F.Cu at (152.4, 34.3)
- added J98: Connectable_Pad_Group_01x02, Protoboard:Connectable_Pad_Group_01x02, F.Cu at (154.9, 34.3)
- D1: footprint Diode_THT:D_DO-41_SOD81_P3.81mm_Vertical_KathodeUp -> Diode_THT:D_DO-41_SOD81_P10.16mm_Horizontal
- R1: value 1K -> 4K7; footprint Resistor_THT:R_Axial_DIN0207_L6.3mm_D2.5mm_P2.54mm_Vertical -> Resistor_THT:R_Axial_DIN0207_L6.3mm_D2.5mm_P10.16mm_Horizontal
- moved R1 12.0 mm to (94.6, 69.4)
- moved D2 2.54 mm to (97.8, 74.9), turned to 180 degrees
- moved C1 1.80 mm to (185.4, 57.1), turned to 0 degrees
- moved D1 1.34 mm to (97.8, 69.4)
- renumbered J135 to J10, J80 to J100, J114 to J101, J152 to J102, J35 to J104, J81 to J105, J115 to J106, J153 to J107, J36 to J108, J82 to J109, J116 to J110, J154 to J111, J37 to J114, J83 to J115, J117 to J116, J155 to J117, J59 to J118, J131 to J119, J55 to J12, J38 to J120, J84 to J121, J118 to J122, J156 to J123, J39 to J125, J85 to J126, J119 to J127, J157 to J128, J40 to J130, J86 to J131, J120 to J132, J158 to J133, J41 to J135, J87 to J136, J121 to J137, J159 to J138, J127 to J14, J42 to J140, J88 to J141, J122 to J142, J160 to J143, J60 to J144, J132 to J145, J43 to J147, J89 to J148, J123 to J149, J161 to J150, J44 to J155, J90 to J156, J124 to J157, J162 to J158, J45 to J160, J91 to J161, J125 to J162, J46 to J164, J92 to J165, J126 to J166, J164 to J167, J18 to J17, J133 to J174, J165 to J175, J3 to J176, J9 to J177, J11 to J178, J47 to J179, J64 to J18, J51 to J180, J93 to J181, J4 to J182, J10 to J183, J12 to J184, J48 to J185, J52 to J186, J94 to J187, J6 to J188, J15 to J189, J98 to J19, J61 to J190, J134 to J191, J166 to J192, J1 to J199, J136 to J20, J7 to J200, J13 to J201, J49 to J202, J53 to J203, J95 to J204, J2 to J205, J8 to J206, J14 to J207, J50 to J208, J54 to J209, J19 to J21, J96 to J210, J5 to J211, J16 to J212, J62 to J213, J65 to J22, J99 to J23, J137 to J24, J20 to J26, J66 to J27, J100 to J28, J138 to J29, J21 to J31, J67 to J32, J101 to J33, J139 to J34, J22 to J36, J68 to J37, J102 to J38, J140 to J39, J56 to J40, J128 to J41, J23 to J43, J69 to J44, J103 to J45, J141 to J46, J24 to J48, J70 to J49, J104 to J50, J142 to J51, J25 to J52, J71 to J53, J105 to J54, J143 to J55, J26 to J57, J72 to J58, J106 to J59, J144 to J60, J27 to J63, J73 to J64, J107 to J65, J145 to J66, J57 to J67, J129 to J68, J28 to J69, J17 to J7, J74 to J70, J108 to J71, J146 to J72, J29 to J74, J109 to J76, J147 to J77, J30 to J78, J76 to J79, J63 to J8, J110 to J80, J148 to J81, J31 to J82, J77 to J83, J111 to J84, J149 to J85, J32 to J87, J78 to J88, J112 to J89, J97 to J9, J150 to J90, J58 to J92, J130 to J93, J33 to J94, J79 to J95, J113 to J96, J151 to J97, J34 to J99, RV2 to RV1, RV3 to RV2, RV5 to RV3, RV1 to RV4, RV4 to RV5, SW1 to SW10, SW4 to SW11, SW6 to SW12, SW2 to SW4, SW3 to SW5, SW5 to SW6
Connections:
- net Net-(D1-A) renamed /12V_Input
- R1 pad 1: +12V -> Net-(D2-A)
- R1 pad 2: Net-(D2-A) -> +12V
- RV1 pad MP: unconnected-(RV2-MountPin) -> (no net)
- RV2 pad MP: unconnected-(RV3-MountPin) -> (no net)
- RV3 pad MP: unconnected-(RV5-MountPin) -> (no net)
- RV4 pad MP: unconnected-(RV1-MountPin) -> (no net)
- RV5 pad MP: unconnected-(RV4-MountPin) -> (no net)
- RV6 pad MP: unconnected-(RV6-MountPin) -> (no net)
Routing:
- net GND: track 501.9 -> 248.9 mm
- net +12V: track 328.1 -> 388.3 mm
- net unconnected-(J8-Pad1): track 55.6 -> 7.62 mm
- net (no net): track 76.2 -> 48.0 mm
- net /12V_Input: track 124.0 -> 117.8 mm
- net unconnected-(J1-Pad1): track 0.00 -> 5.12 mm
- net unconnected-(J4-Pad1): track 0.00 -> 5.06 mm
- net unconnected-(J3-Pad1): track 0.00 -> 5.06 mm
- net unconnected-(J2-Pad1): track 0.00 -> 5.06 mm
- net unconnected-(J98-Pad1): track 0.00 -> 5.05 mm
- net unconnected-(J91-Pad1): track 0.00 -> 5.05 mm
- net unconnected-(J86-Pad1): track 0.00 -> 5.05 mm
- net unconnected-(J73-Pad1): track 0.00 -> 5.05 mm
- net unconnected-(J62-Pad1): track 0.00 -> 5.05 mm
- net unconnected-(J61-Pad1): track 0.00 -> 5.05 mm
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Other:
- board text added: "TODO LIST - Imported symbol to replace - Pass DRC (already pass the important parts)"
- board text removed: "TODO LIST - Bonus pads not on the schematic - Imported symbol to replace - Rotary encoder?? - Remake the cursed footprints - Redo schematic - Have 3D models - Can I fit in MORE knobs? - Use proper net width (sounds complicated) - Pass DRC lol"

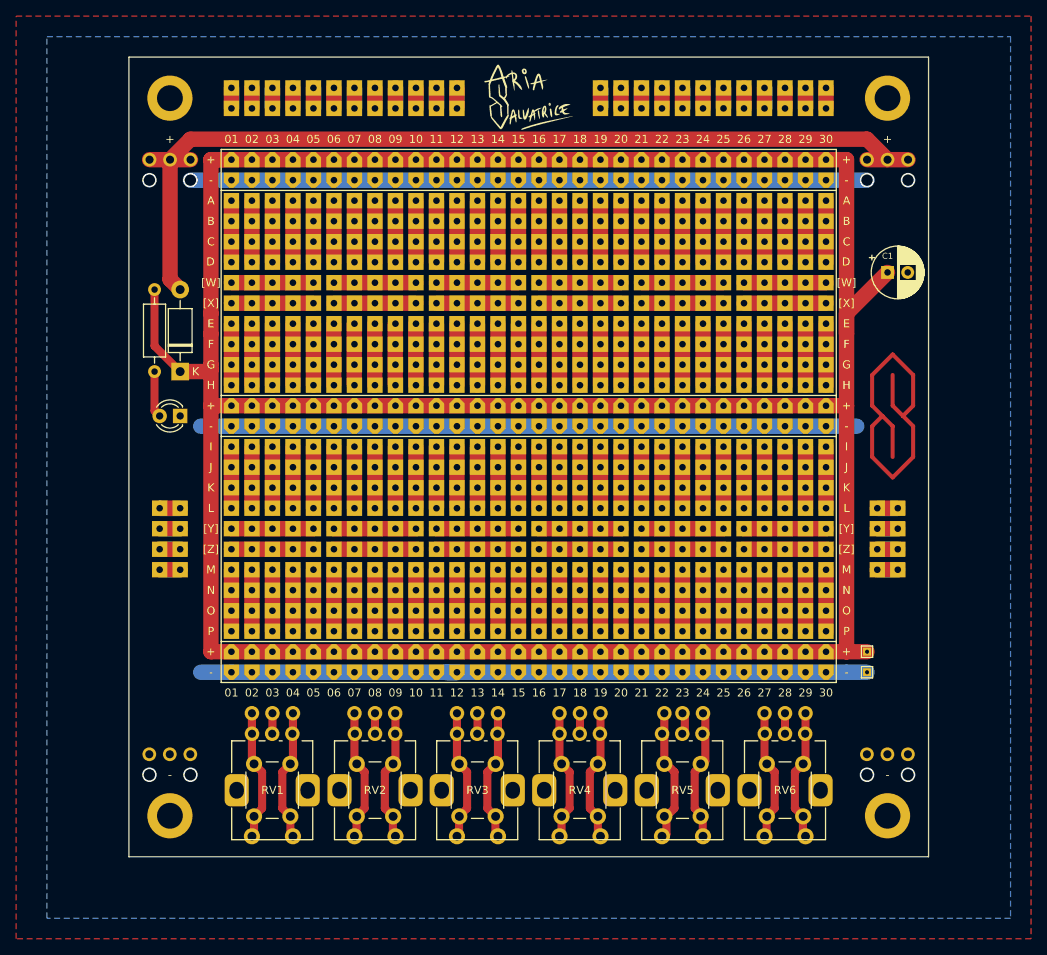
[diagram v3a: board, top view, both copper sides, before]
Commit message: Proto silkscreen adjust, gitignore gerbers
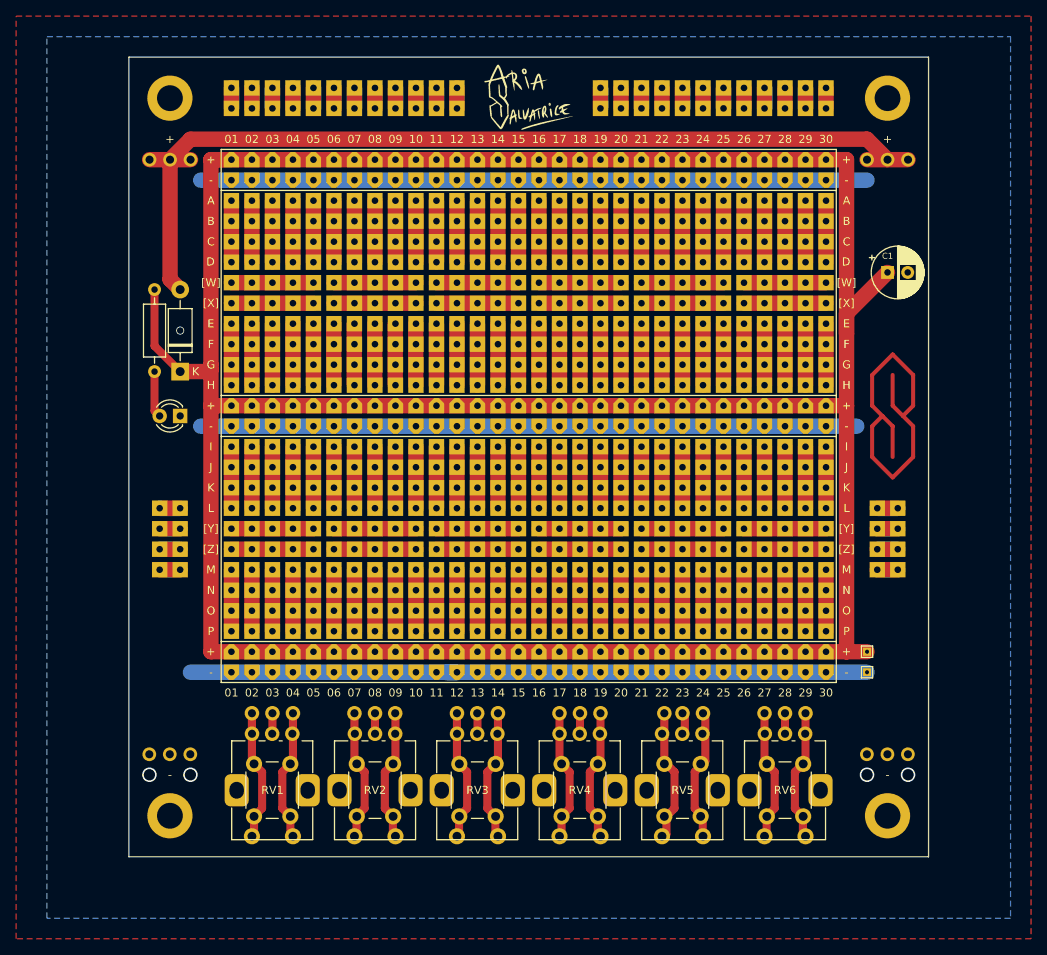
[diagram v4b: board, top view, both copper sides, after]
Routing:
- net GND: vias 8 -> 5
